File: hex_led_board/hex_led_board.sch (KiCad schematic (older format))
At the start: 90 parts, among them J1 Conn_01x04, J2 Conn_01x04

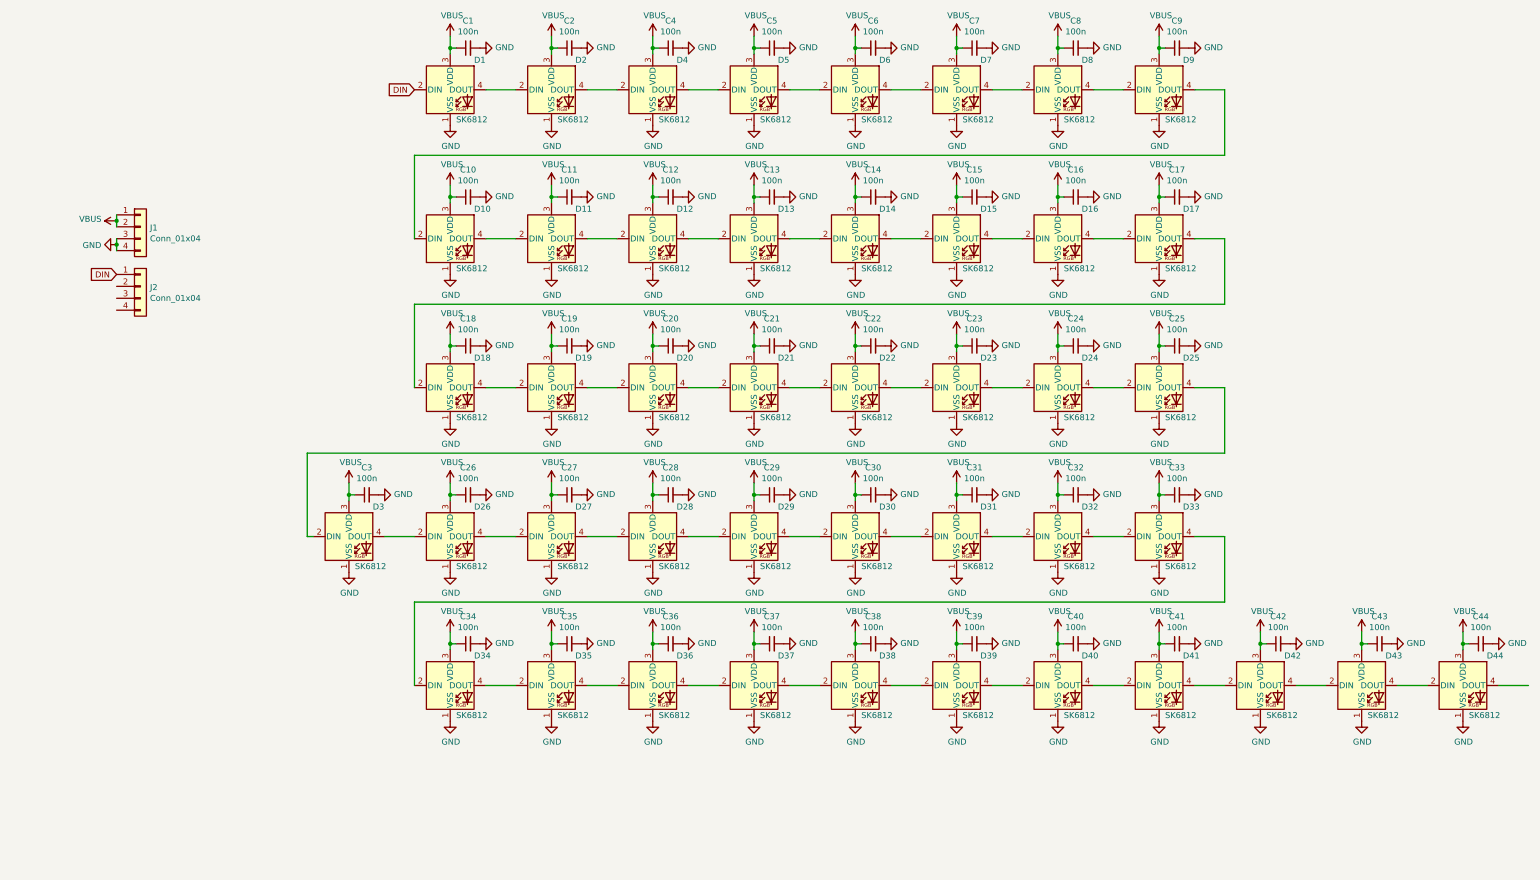
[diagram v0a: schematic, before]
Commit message: finished led board
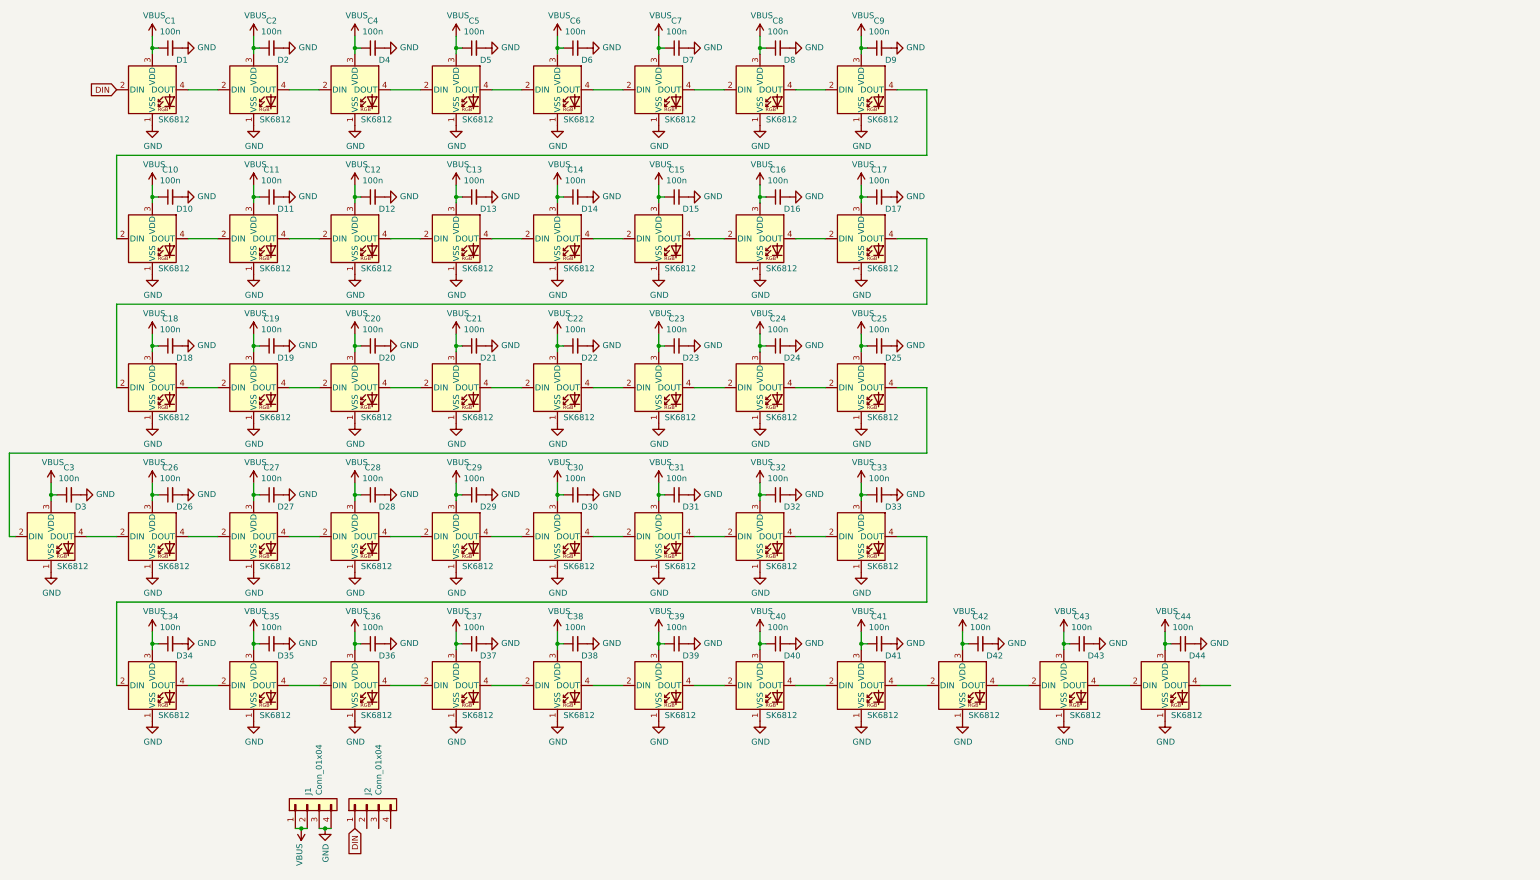
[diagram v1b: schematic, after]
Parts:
- J1, J2: footprint Connector_PinHeader_2.00mm:PinHeader_1x04_P2.00mm_Vertical_SMD_Pin1Left -> Connector_PinHeader_2.54mm:PinHeader_1x04_P2.54mm_Vertical_SMD_Pin1Left
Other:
- moved on the sheet: C1, C10, C11, C12, C13, C14, C15, C16, C17, C18, C19, C2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
